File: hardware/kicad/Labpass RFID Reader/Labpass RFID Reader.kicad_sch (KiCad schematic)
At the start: 1 part, among them U1 adafruit_huzzah_32

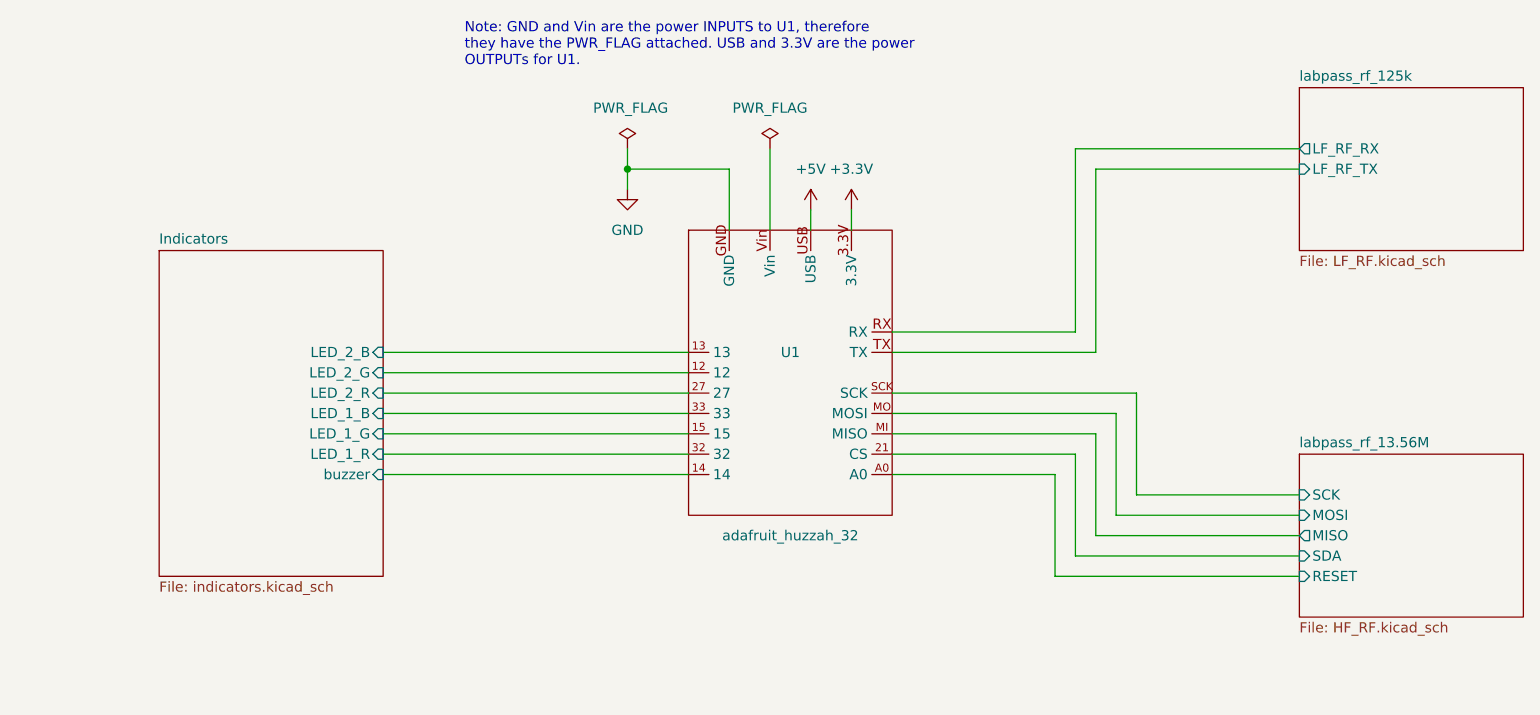
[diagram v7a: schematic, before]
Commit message: Additional Changes
* remove transistor on LF path and power coil directly
  from ESP TX pin at 3.3V
* add some test points around the HF path
* add some cheap pots on LF for tuning the amplifier bias
  and comparator threshold
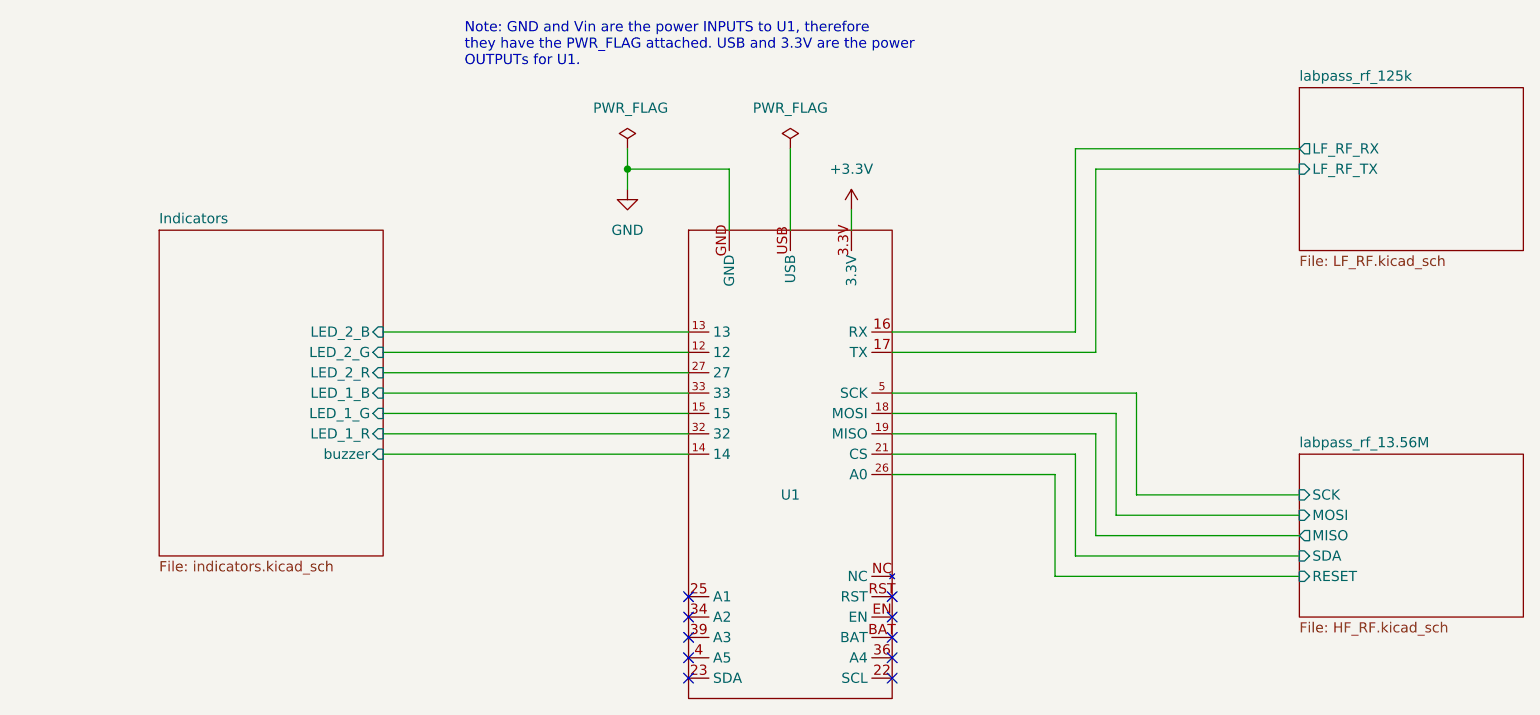
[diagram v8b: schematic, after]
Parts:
- U1: value adafruit_huzzah_32 -> (none); footprint Capstone Footprint Library:adafruit_huzzah_32 -> (none)
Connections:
- net labpass_rf_125k/LF_RF_RX: now also U1.16 (RX); no longer U1.RX
- net labpass_rf_125k/LF_RF_TX: now also U1.17 (TX); no longer U1.TX
- net labpass_rf_13.56M/MISO: now also U1.19 (MISO); no longer U1.MI (MISO)
- net labpass_rf_13.56M/MOSI: now also U1.18 (MOSI); no longer U1.MO (MOSI)
- net labpass_rf_13.56M/RESET: now also U1.26 (A0); no longer U1.A0
- net labpass_rf_13.56M/SCK: now also U1.5 (SCK); no longer U1.SCK
- net +5V: no longer names the net of U1.USB
- no-connect marks 0 -> 10
